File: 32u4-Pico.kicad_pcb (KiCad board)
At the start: 2 copper layers, 21.3 x 51.3 mm, 27 parts, among them J3 2.54mm header 01x20, J4 2.54mm header 01x20, U1 ATmega32U4-MU, Y1 8MHz 3225_4p crystal

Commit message: smol fix-y
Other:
- net class Default removed
- net class USB_DIFF_90 removed

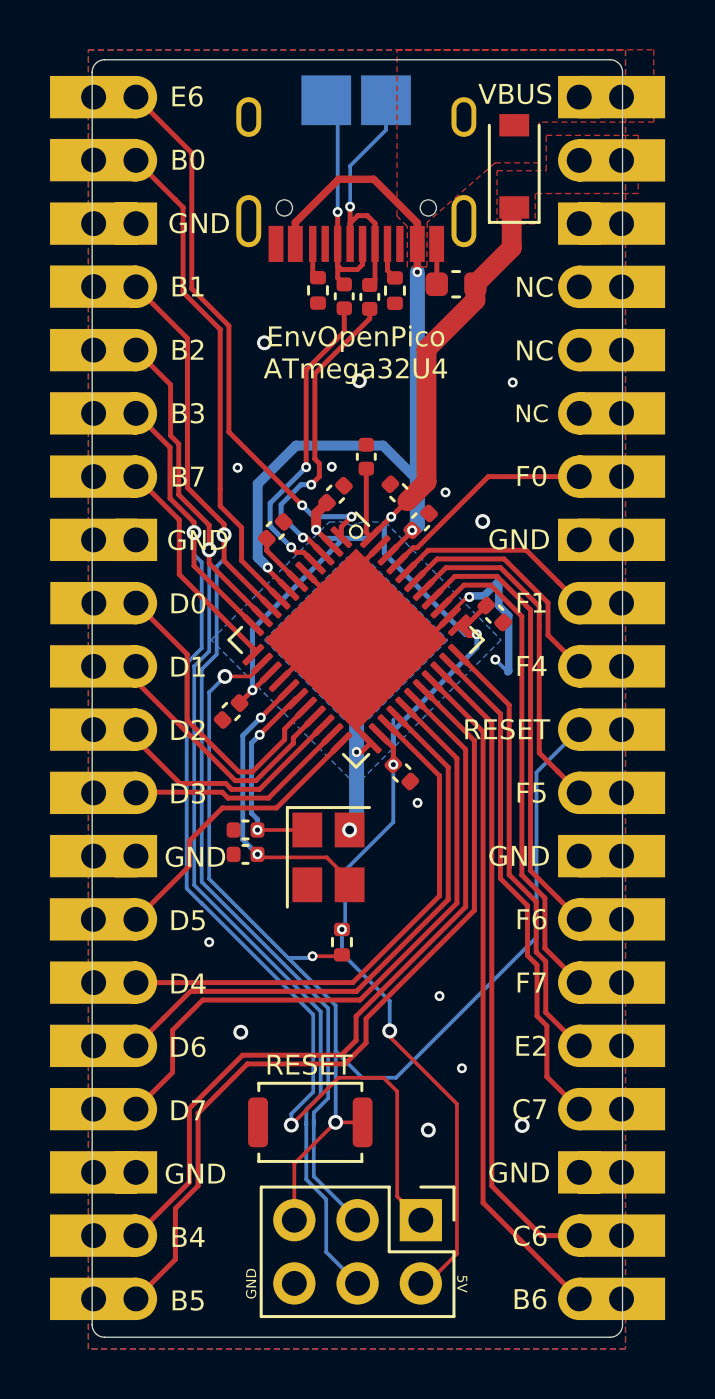
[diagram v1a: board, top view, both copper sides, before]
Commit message: change some egregious design choices
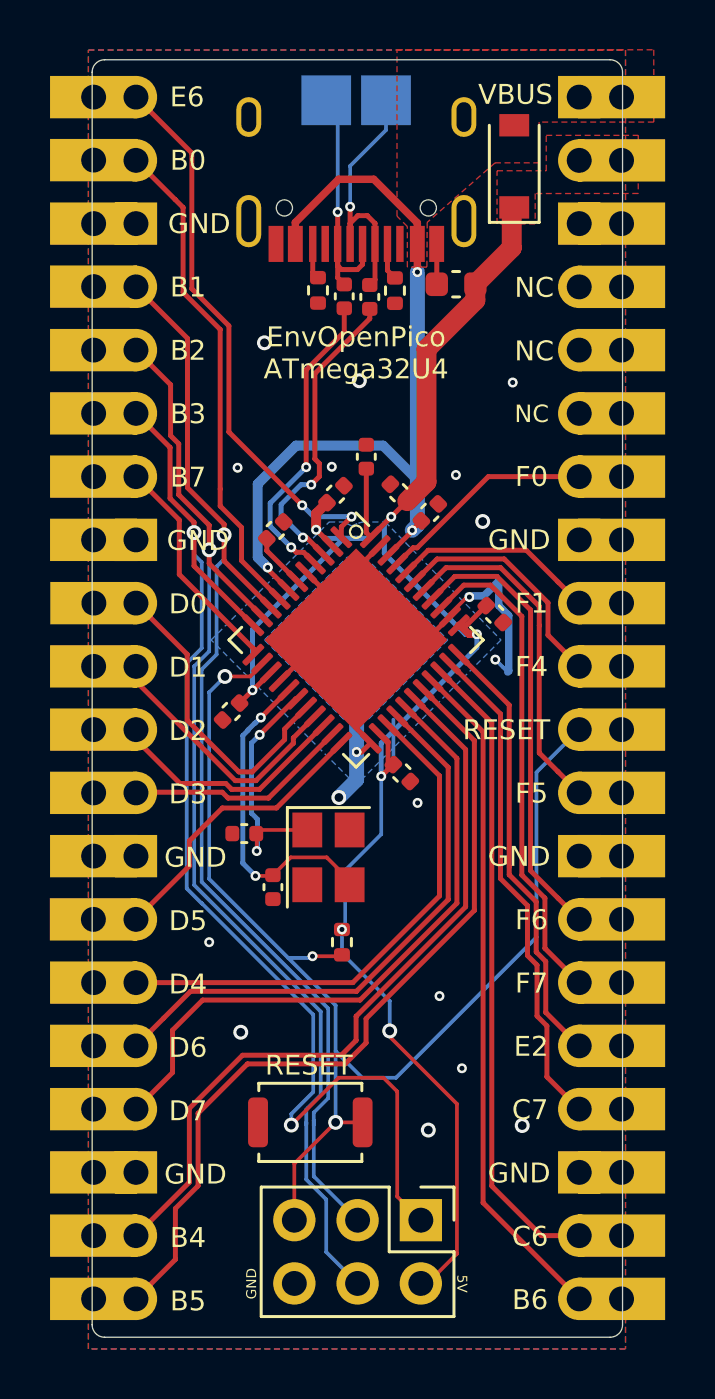
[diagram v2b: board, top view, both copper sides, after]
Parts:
- moved C7 1.71 mm to (100.2, 90.5), turned to 90 degrees
- moved C3 0.53 mm to (106.5, 75.4)
- moved C2 0.15 mm to (99.1, 88.3)
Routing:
- net XTAL1: track 8.17 -> 9.83 mm
- net XTAL2: track 11.9 -> 13.1 mm
- net VSYS: track 78.6 -> 79.7 mm
- net GND: track 35.4 -> 34.3 mm
- net VBUS: track 35.5 -> 36.1 mm
